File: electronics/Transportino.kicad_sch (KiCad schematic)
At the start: 63 parts, among them J1 MOTOR_A_0, J2 MOTOR_A_1, J3 MOTOR_B_0, J4 MOTOR_B_1, J5 USB_B_Micro, SW1 PROG, SW2 SW_DPDT_x2, U1 RP2040, U2 TB6612FNG, U3 W25Q128JVS, U4 MPU-6050, U5 LM2575BU-ADJ, U6 NCP1117-3.3_SOT223, Y1 12Mhz

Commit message: Added ros part
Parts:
- H1, H2, H3, H4: footprint MountingHole:MountingHole_2.2mm_M2 -> MountingHole:MountingHole_2.7mm_M2.5
- TP1, TP2, TP3: renamed from TP?; footprint (none) -> TestPoint:TestPoint_Pad_D1.0mm
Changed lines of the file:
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@@
   (symbol (lib_id "power:+12V") (at 247.65 250.19 180) (unit 1)
     (in_bom yes) (on_board yes) (fields_autoplaced)
-    (property "Reference" "#PWR?" (id 0) (at 247.65 246.38 0)
+    (property "Reference" "#PWR0127" (id 0) (at 247.65 246.38 0)
       (effects (font (size 1.27 1.27)) hide)
     )
@@
       (effects (font (size 1.27 1.27)) (justify left))
     )
-    (property "Footprint" "MountingHole:MountingHole_2.2mm_M2" (id 2) (at 111.76 259.08 0)
+    (property "Footprint" "MountingHole:MountingHole_2.7mm_M2.5" (id 2) (at 111.76 259.08 0)
       (effects (font (size 1.27 1.27)) hide)
     )
@@
       (effects (font (size 1.27 1.27)) (justify left))
     )
-    (property "Footprint" "MountingHole:MountingHole_2.2mm_M2" (id 2) (at 132.08 259.08 0)
+    (property "Footprint" "MountingHole:MountingHole_2.7mm_M2.5" (id 2) (at 132.08 259.08 0)
       (effects (font (size 1.27 1.27)) hide)
     )
@@
   (symbol (lib_id "Connector:TestPoint") (at 231.14 250.19 0) (unit 1)
     (in_bom yes) (on_board yes) (fields_autoplaced)
-    (property "Reference" "TP?" (id 0) (at 233.68 245.6179 0)
+    (property "Reference" "TP1" (id 0) (at 233.68 245.6179 0)
       (effects (font (size 1.27 1.27)) (justify left))
     )
@@
       (effects (font (size 1.27 1.27)) (justify left))
     )
-    (property "Footprint" "" (id 2) (at 236.22 250.19 0)
+    (property "Footprint" "TestPoint:TestPoint_Pad_D1.0mm" (id 2) (at 236.22 250.19 0)
       (effects (font (size 1.27 1.27)) hide)
     )
@@
   (symbol (lib_id "Connector:TestPoint") (at 247.65 250.19 0) (unit 1)
     (in_bom yes) (on_board yes) (fields_autoplaced)
-    (property "Reference" "TP?" (id 0) (at 250.19 245.6179 0)
+    (property "Reference" "TP3" (id 0) (at 250.19 245.6179 0)
       (effects (font (size 1.27 1.27)) (justify left))
     )
@@
       (effects (font (size 1.27 1.27)) (justify left))
     )
-    (property "Footprint" "" (id 2) (at 252.73 250.19 0)
+    (property "Footprint" "TestPoint:TestPoint_Pad_D1.0mm" (id 2) (at 252.73 250.19 0)
       (effects (font (size 1.27 1.27)) hide)
     )
@@
       (effects (font (size 1.27 1.27)) (justify left))
     )
-    (property "Footprint" "MountingHole:MountingHole_2.2mm_M2" (id 2) (at 152.4 257.81 0)
+    (property "Footprint" "MountingHole:MountingHole_2.7mm_M2.5" (id 2) (at 152.4 257.81 0)
       (effects (font (size 1.27 1.27)) hide)
     )
@@
   (symbol (lib_id "Connector:TestPoint") (at 240.03 262.89 0) (unit 1)
     (in_bom yes) (on_board yes) (fields_autoplaced)
-    (property "Reference" "TP?" (id 0) (at 242.57 258.3179 0)
+    (property "Reference" "TP2" (id 0) (at 242.57 258.3179 0)
       (effects (font (size 1.27 1.27)) (justify left))
     )
@@
       (effects (font (size 1.27 1.27)) (justify left))
     )
-    (property "Footprint" "" (id 2) (at 245.11 262.89 0)
+    (property "Footprint" "TestPoint:TestPoint_Pad_D1.0mm" (id 2) (at 245.11 262.89 0)
       (effects (font (size 1.27 1.27)) hide)
     )
@@
   (symbol (lib_id "power:+3.3V") (at 240.03 262.89 180) (unit 1)
     (in_bom yes) (on_board yes) (fields_autoplaced)
-    (property "Reference" "#PWR?" (id 0) (at 240.03 259.08 0)
+    (property "Reference" "#PWR0126" (id 0) (at 240.03 259.08 0)
       (effects (font (size 1.27 1.27)) hide)
     )
@@
       (effects (font (size 1.27 1.27)) (justify left))
     )
-    (property "Footprint" "MountingHole:MountingHole_2.2mm_M2" (id 2) (at 92.71 257.81 0)
+    (property "Footprint" "MountingHole:MountingHole_2.7mm_M2.5" (id 2) (at 92.71 257.81 0)
       (effects (font (size 1.27 1.27)) hide)
     )
@@
       (reference "#PWR0125") (unit 1) (value "+3V3") (footprint "")
     )
+    (path "/f52161a0-f4fe-4469-bc3c-f014e7fd5873"
+      (reference "#PWR0126") (unit 1) (value "+3.3V") (footprint "")
+    )
     (path "/20ac7f1d-5328-42f9-b97e-8392aa4624bf"
-      (reference "#PWR?") (unit 1) (value "+12V") (footprint "")
-    )
-    (path "/f52161a0-f4fe-4469-bc3c-f014e7fd5873"
-      (reference "#PWR?") (unit 1) (value "+3.3V") (footprint "")
+      (reference "#PWR0127") (unit 1) (value "+12V") (footprint "")
     )
     (path "/897e7ab0-9b87-49aa-9009-a8e87aac9abb"
@@
     )
     (path "/f85a0141-6ff4-45de-aae6-298fd70a046a"
-      (reference "H1") (unit 1) (value "MountingHole") (footprint "MountingHole:MountingHole_2.2mm_M2")
+      (reference "H1") (unit 1) (value "MountingHole") (footprint "MountingHole:MountingHole_2.7mm_M2.5")
     )
     (path "/66841c31-c845-4c94-96cd-2a7b74adbe0c"
-      (reference "H2") (unit 1) (value "MountingHole") (footprint "MountingHole:MountingHole_2.2mm_M2")
+      (reference "H2") (unit 1) (value "MountingHole") (footprint "MountingHole:MountingHole_2.7mm_M2.5")
     )
     (path "/7b305265-4180-420c-8e15-e9ce60952f03"
-      (reference "H3") (unit 1) (value "MountingHole") (footprint "MountingHole:MountingHole_2.2mm_M2")
+      (reference "H3") (unit 1) (value "MountingHole") (footprint "MountingHole:MountingHole_2.7mm_M2.5")
     )
     (path "/d1097040-5da8-496e-9ca2-6633d62b2369"
-      (reference "H4") (unit 1) (value "MountingHole") (footprint "MountingHole:MountingHole_2.2mm_M2")
+      (reference "H4") (unit 1) (value "MountingHole") (footprint "MountingHole:MountingHole_2.7mm_M2.5")
     )
     (path "/a19b516a-dc44-4576-a1ab-73e76e6f3f6f"
@@
     )
     (path "/9826bb83-0155-4d11-a9af-8e66989debcc"
-      (reference "TP?") (unit 1) (value "TestPoint") (footprint "")
+      (reference "TP1") (unit 1) (value "TestPoint") (footprint "TestPoint:TestPoint_Pad_D1.0mm")
+    )
+    (path "/f01d4561-db8e-400b-b14c-0fc04801d7f5"
+      (reference "TP2") (unit 1) (value "TestPoint") (footprint "TestPoint:TestPoint_Pad_D1.0mm")
     )
     (path "/c77cc684-6d7d-40ca-80fb-70970ffcddef"
-      (reference "TP?") (unit 1) (value "TestPoint") (footprint "")
-    )
-    (path "/f01d4561-db8e-400b-b14c-0fc04801d7f5"
-      (reference "TP?") (unit 1) (value "TestPoint") (footprint "")
+      (reference "TP3") (unit 1) (value "TestPoint") (footprint "TestPoint:TestPoint_Pad_D1.0mm")
     )
     (path "/57fde7d1-ea1d-4cdd-9e7c-ae005a61eb86"

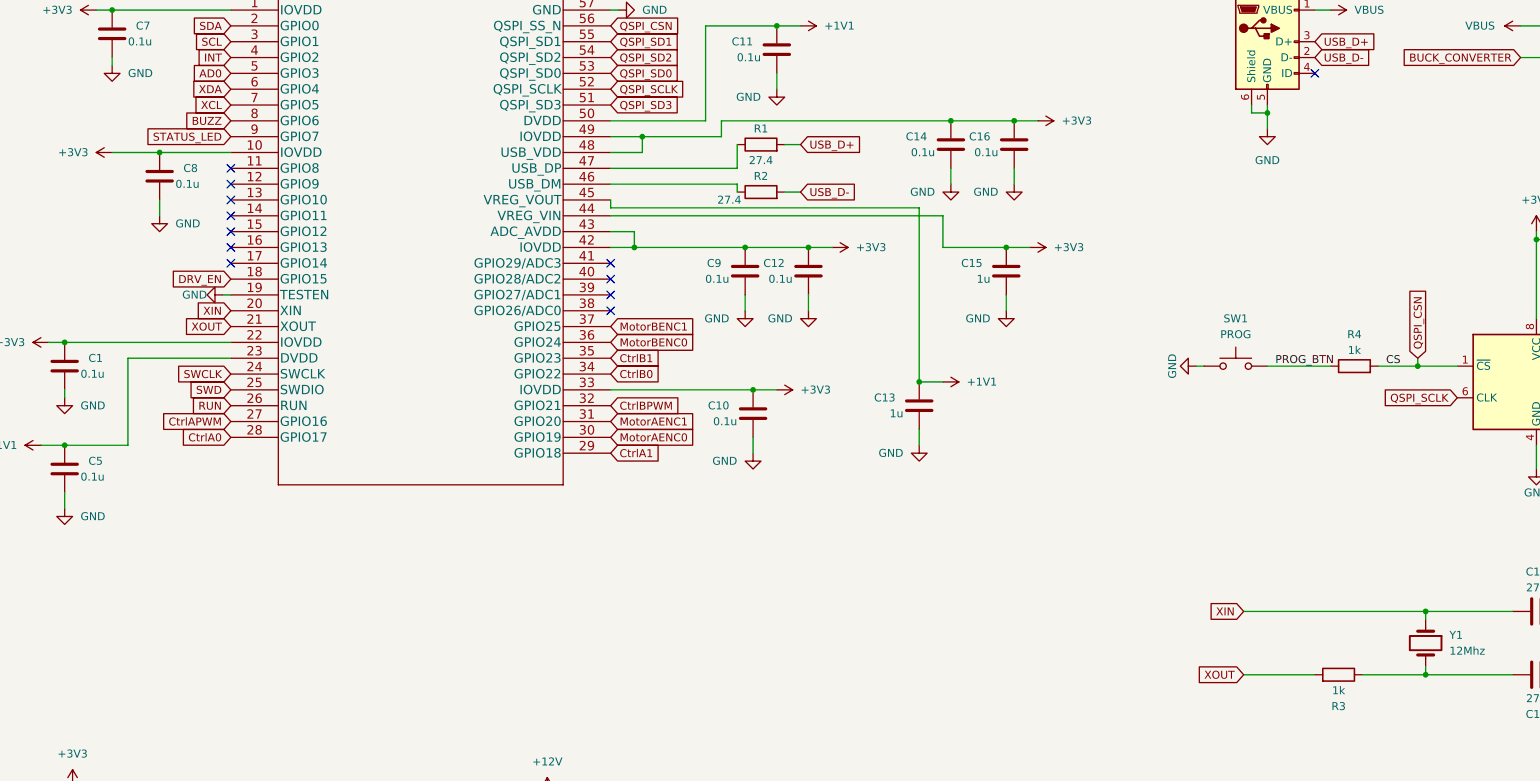
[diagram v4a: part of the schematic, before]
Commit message: Changed buzzer gpio pin.
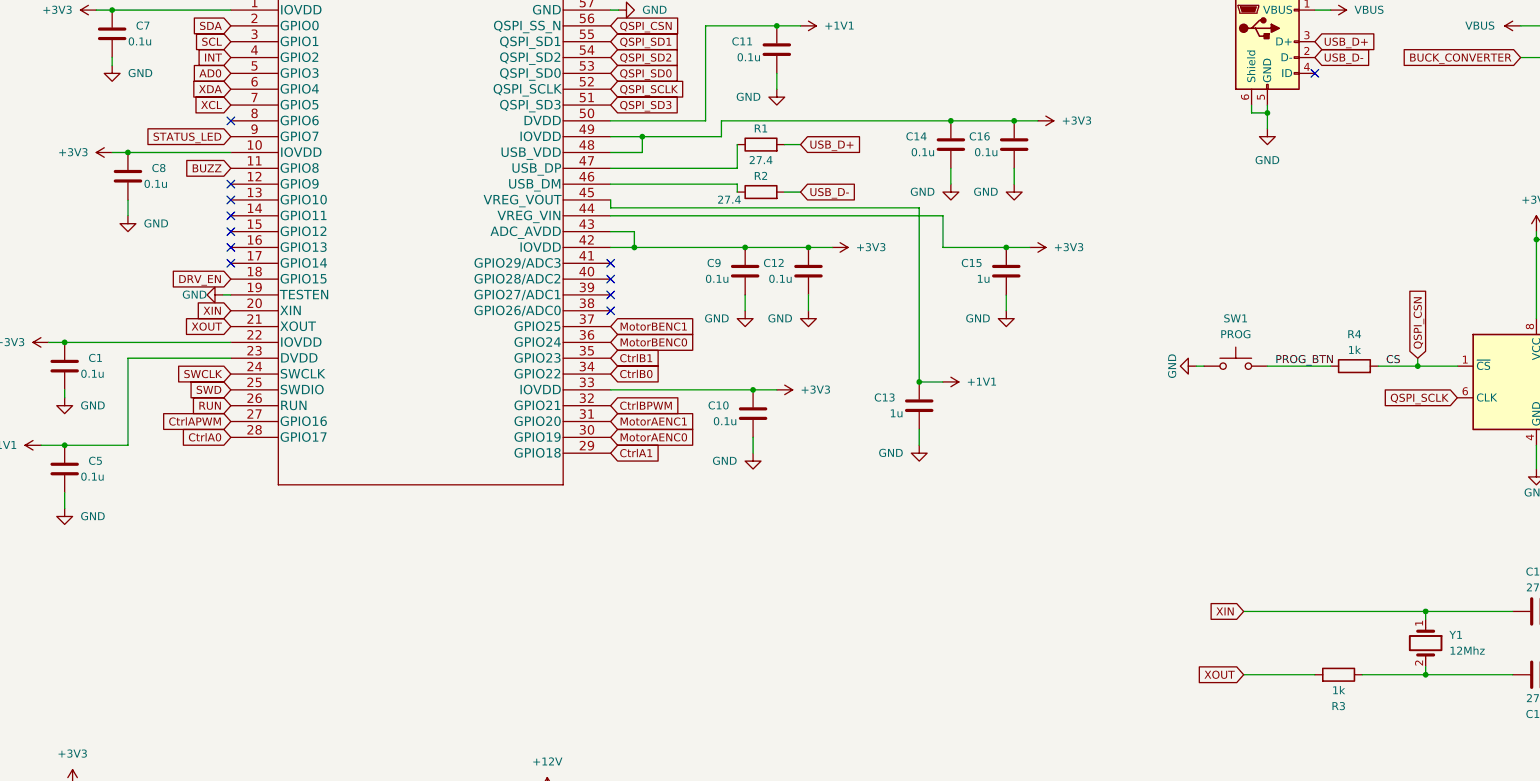
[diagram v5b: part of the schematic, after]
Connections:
- net BUZZ: now also U1.11 (GPIO8); no longer U1.8 (GPIO6)
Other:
- moved on the sheet: C8
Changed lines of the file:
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@@
   (junction (at 40.64 158.75) (diameter 0) (color 0 0 0 0)
   )
+  (junction (at 43.18 53.34) (diameter 0) (color 0 0 0 0)
+  )
   (junction (at 284.48 137.16) (diameter 0) (color 0 0 0 0)
   )
@@
   (junction (at 226.06 46.99) (diameter 0) (color 0 0 0 0)
   )
-  (junction (at 48.26 53.34) (diameter 0) (color 0 0 0 0)
-  )
   (junction (at 251.46 137.16) (diameter 0) (color 0 0 0 0)
   )
@@
   (junction (at 384.81 100.33) (diameter 0) (color 0 0 0 0)
   )
+  (no_connect (at 59.69 48.26))
   (no_connect (at 233.68 40.64))
   (no_connect (at 59.69 66.04))
@@
   (no_connect (at 59.69 63.5))
   (no_connect (at 59.69 60.96))
-  (no_connect (at 59.69 55.88))
   (no_connect (at 59.69 58.42))
   (wire (pts (xy 99.06 166.37) (xy 99.06 171.45))
@@
     (stroke (width 0) (type default) (color 0 0 0 0))
   )
-  (wire (pts (xy 48.26 53.34) (xy 59.69 53.34))
-    (stroke (width 0) (type default) (color 0 0 0 0))
-  )
   (wire (pts (xy 143.51 99.06) (xy 143.51 101.6))
     (stroke (width 0) (type default) (color 0 0 0 0))
@@
     (stroke (width 0) (type default) (color 0 0 0 0))
   )
-  (wire (pts (xy 48.26 60.96) (xy 48.26 63.5))
+  (wire (pts (xy 43.18 60.96) (xy 43.18 63.5))
     (stroke (width 0) (type default) (color 0 0 0 0))
   )
@@
     (stroke (width 0) (type default) (color 0 0 0 0))
   )
+  (wire (pts (xy 43.18 53.34) (xy 59.69 53.34))
+    (stroke (width 0) (type default) (color 0 0 0 0))
+  )
   (wire (pts (xy 273.05 137.16) (xy 284.48 137.16))
     (stroke (width 0) (type default) (color 0 0 0 0))
@@
     (stroke (width 0) (type default) (color 0 0 0 0))
   )
-  (wire (pts (xy 40.64 53.34) (xy 48.26 53.34))
+  (wire (pts (xy 40.64 53.34) (xy 43.18 53.34))
     (stroke (width 0) (type default) (color 0 0 0 0))
   )
@@
     )
   )
-  (global_label "BUZZ" (shape input) (at 59.69 48.26 180) (fields_autoplaced)
-    (effects (font (size 1.27 1.27)) (justify right))
-    (property "Intersheet References" "${INTERSHEET_REFS}" (id 0) (at 52.2574 48.1806 0)
-      (effects (font (size 1.27 1.27)) (justify right) hide)
-    )
-  )
   (global_label "MotorAENC0" (shape input) (at 120.65 99.06 0) (fields_autoplaced)
     (effects (font (size 1.27 1.27)) (justify left))
@@
     (property "Intersheet References" "${INTERSHEET_REFS}" (id 0) (at 128.8083 101.6794 0)
       (effects (font (size 1.27 1.27)) (justify left) hide)
+    )
+  )
+  (global_label "BUZZ" (shape input) (at 59.69 55.88 180) (fields_autoplaced)
+    (effects (font (size 1.27 1.27)) (justify right))
+    (property "Intersheet References" "${INTERSHEET_REFS}" (id 0) (at 52.2574 55.8006 0)
+      (effects (font (size 1.27 1.27)) (justify right) hide)
     )
   )
@@
     (pin "3")
   )
-  (symbol (lib_id "Device:C") (at 48.26 57.15 180) (unit 1)
-    (in_bom yes) (on_board yes)
-    (property "Reference" "C8" (id 0) (at 52.07 55.88 0)
-      (effects (font (size 1.27 1.27)) (justify right))
-    )
-    (property "Value" "0.1u" (id 1) (at 50.8 58.42 0)
-      (effects (font (size 1.27 1.27)) (justify right))
-    )
-    (property "Footprint" "Capacitor_SMD:C_1206_3216Metric" (id 2) (at 47.2948 53.34 0)
-      (effects (font (size 1.27 1.27)) hide)
-    )
-    (property "Datasheet" "~" (id 3) (at 48.26 57.15 0)
+  (symbol (lib_id "Device:C") (at 43.18 57.15 180) (unit 1)
+    (in_bom yes) (on_board yes)
+    (property "Reference" "C8" (id 0) (at 46.99 55.88 0)
+      (effects (font (size 1.27 1.27)) (justify right))
+    )
+    (property "Value" "0.1u" (id 1) (at 45.72 58.42 0)
+      (effects (font (size 1.27 1.27)) (justify right))
+    )
+    (property "Footprint" "Capacitor_SMD:C_1206_3216Metric" (id 2) (at 42.2148 53.34 0)
+      (effects (font (size 1.27 1.27)) hide)
+    )
+    (property "Datasheet" "~" (id 3) (at 43.18 57.15 0)
       (effects (font (size 1.27 1.27)) hide)
     )
@@
     (pin "1")
   )
-  (symbol (lib_id "power:GND") (at 48.26 63.5 0) (unit 1)
-    (in_bom yes) (on_board yes)
-    (property "Reference" "#PWR0118" (id 0) (at 48.26 69.85 0)
-      (effects (font (size 1.27 1.27)) hide)
-    )
-    (property "Value" "GND" (id 1) (at 50.8 64.77 0)
-      (effects (font (size 1.27 1.27)) (justify left))
-    )
-    (property "Footprint" "" (id 2) (at 48.26 63.5 0)
-      (effects (font (size 1.27 1.27)) hide)
-    )
-    (property "Datasheet" "" (id 3) (at 48.26 63.5 0)
-      (effects (font (size 1.27 1.27)) hide)
-    )
+  (symbol (lib_id "power:GND") (at 43.18 63.5 0) (unit 1)
+    (in_bom yes) (on_board yes)
+    (property "Reference" "#PWR0118" (id 0) (at 43.18 69.85 0)
+      (effects (font (size 1.27 1.27)) hide)
+    )
+    (property "Value" "GND" (id 1) (at 45.72 64.77 0)
+      (effects (font (size 1.27 1.27)) (justify left))
+    )
+    (property "Footprint" "" (id 2) (at 43.18 63.5 0)
+      (effects (font (size 1.27 1.27)) hide)
+    )
+    (property "Datasheet" "" (id 3) (at 43.18 63.5 0)
+      (effects (font (size 1.27 1.27)) hide)
+    )
